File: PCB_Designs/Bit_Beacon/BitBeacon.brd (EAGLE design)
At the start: 30.5 x 33 mm, 105 parts, among them IC1 AD8603UJ, IC2 AD8603UJ, IC3 AD8603UJ, IC4 AD8603UJ

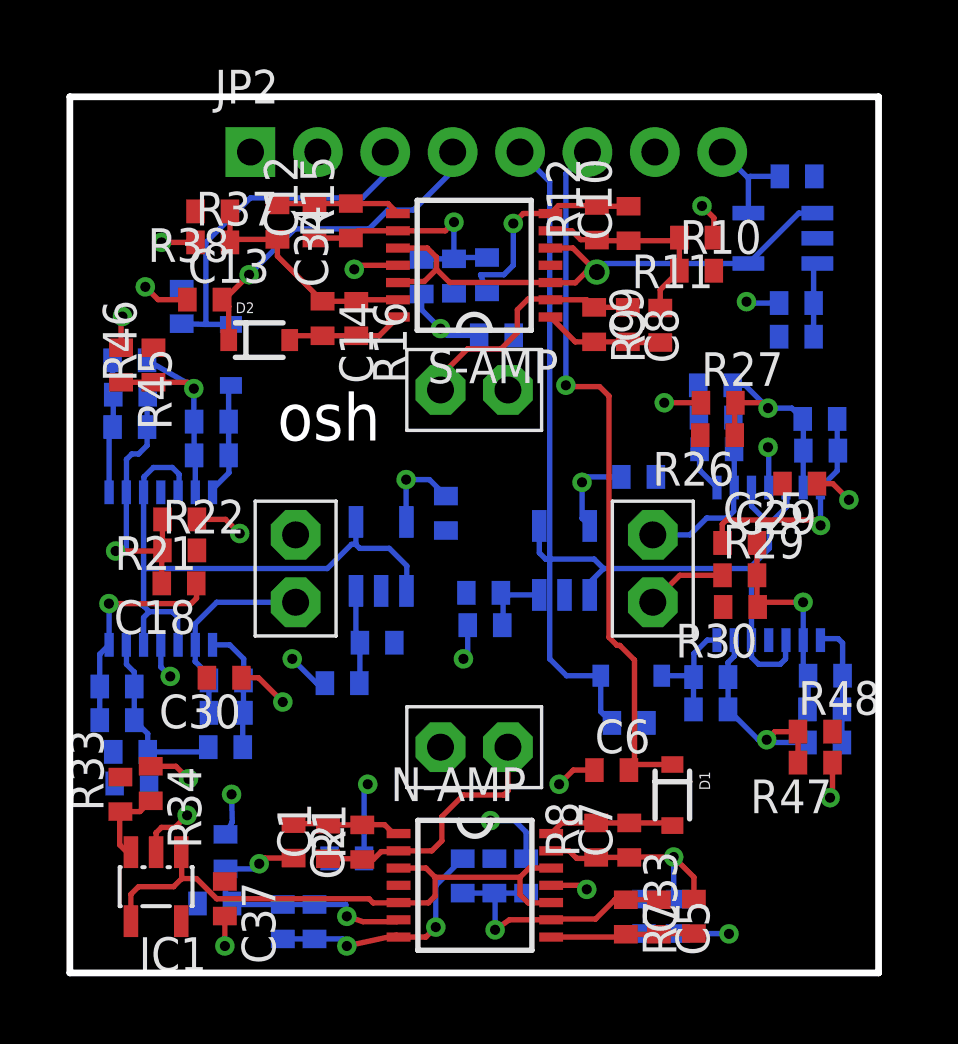
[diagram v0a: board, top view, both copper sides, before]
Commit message: finished and ordered PCB design for Bit Beacon
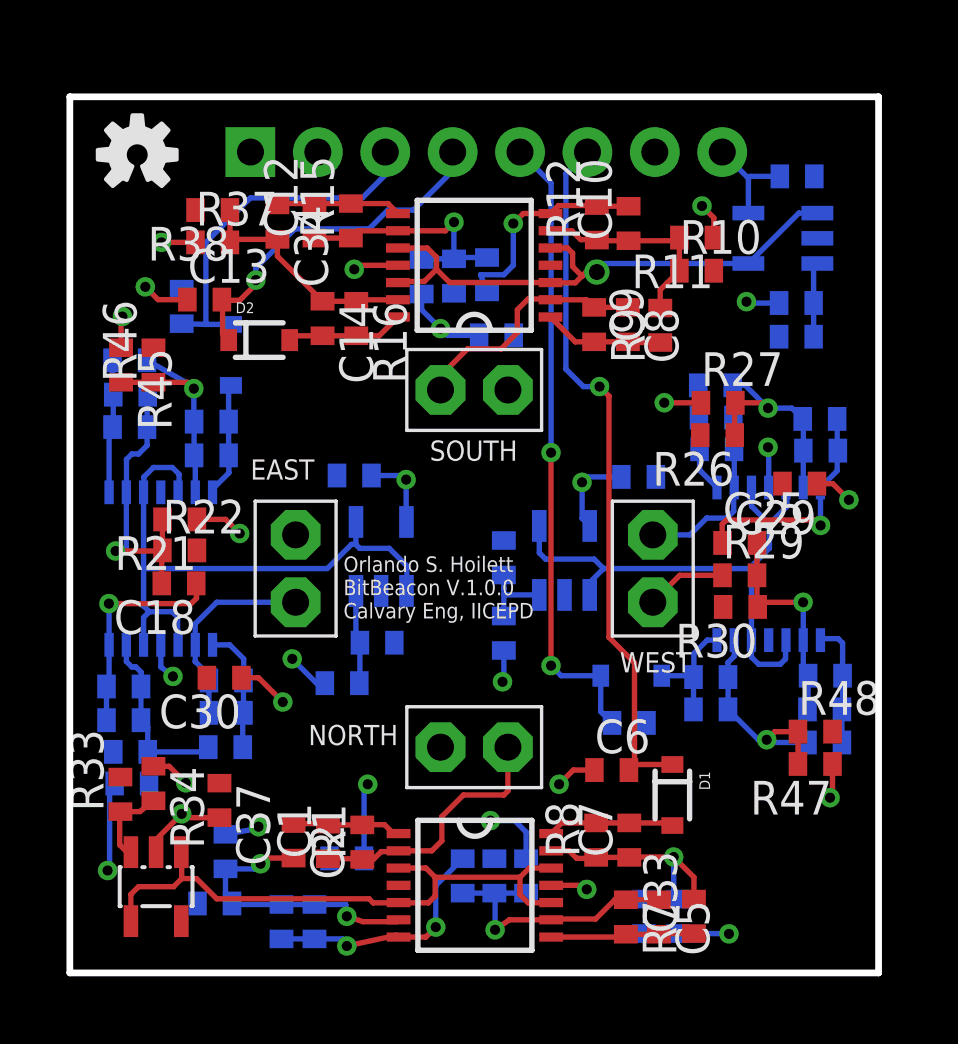
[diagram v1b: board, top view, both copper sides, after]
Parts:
- added LOGO1: OSHW-LOGOS, SparkFun-Aesthetics:OSHW-LOGO-S
- moved C39 3.74 mm to (10.7, 18.7), turned to 0 degrees
- moved C37 3.71 mm to (5.64, 6.50)
- moved R44 1.52 mm to (16.4, 15.6), turned to 270 degrees
- moved R43 0.77 mm to (16.4, 12.8), turned to 270 degrees
- moved C17 0.25 mm to (2.03, 10.8)
- moved R20 0.25 mm to (2.03, 9.53)
- moved R34 0.10 mm to (3.15, 7.14)
- moved C3 0.05 mm to (7.98, 1.93)
- moved R47 0.05 mm to (28.1, 7.87)
- moved R38 0.05 mm to (5.38, 28.8)
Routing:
- net 5V: track 29.8 -> 32.6 mm, vias 12 -> 13
- net GND: track 26.2 -> 26.1 mm, vias 15 -> 14
- net W-OUT: track 23.7 -> 23.8 mm, vias 0 -> 2
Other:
- board text added: "EAST"
- board text added: "NORTH"
- board text added: "Orlando S. Hoilett BitBeacon V.1.0.0 Calvary Eng, IICEPD"
- board text added: "SOUTH"
- board text added: "WEST"
- board text removed: "osh"

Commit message: updating BitBeacon design with a better high pass filter design and started teh BitBeacon_Emitter circuit
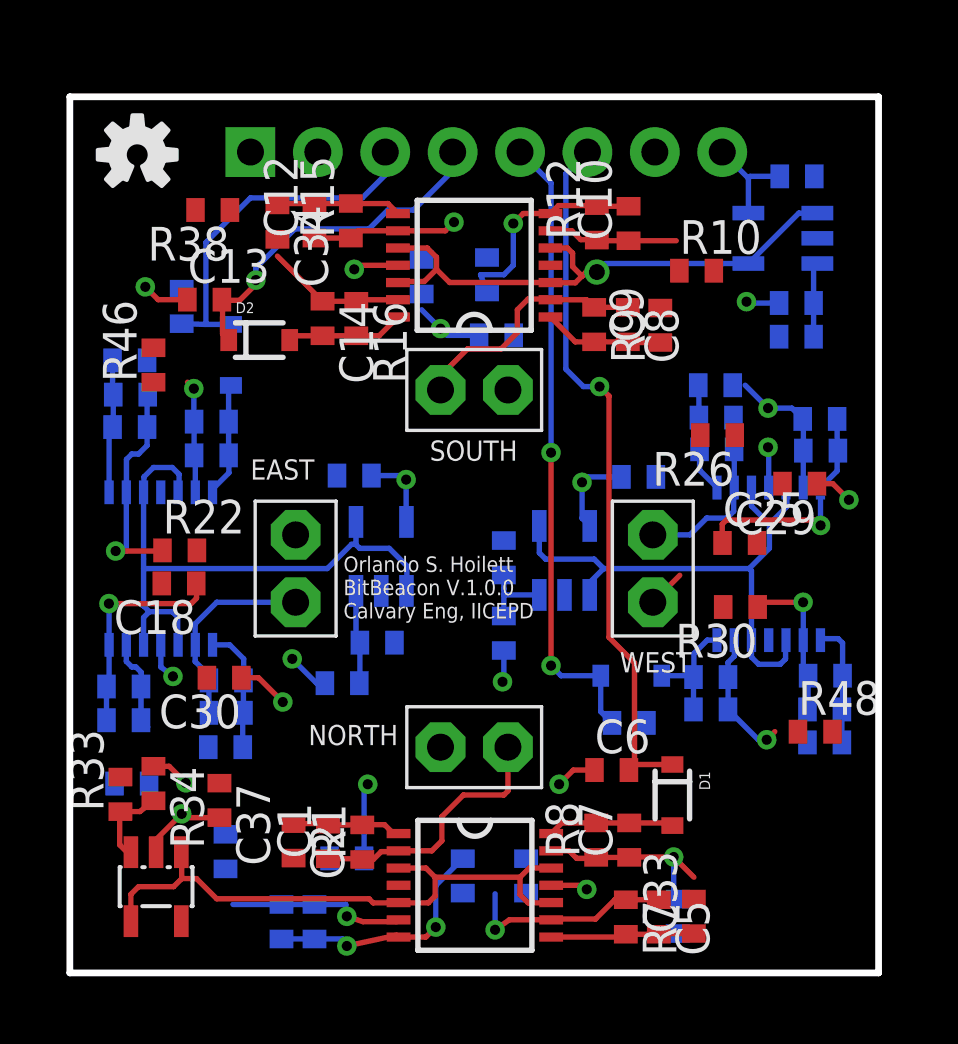
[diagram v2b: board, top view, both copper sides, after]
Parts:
- removed R11, R13, R19, R21, R27, R29, R3, R35, R37, R45, R47, R5: (no value), resistor:R0402
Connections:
- new net N$27: C2.2, R2.2
- new net N$34: C4.2, R6.2
- new net N$35: C33.2, R36.2
- new net N$36: C34.2, R38.2
- new net N$37: C11.2, R14.2
- new net N$38: C9.2, R10.2
- new net N$39: C35.2, R46.2
- new net N$40: C18.2, R22.2
- new net N$41: C16.2, R18.2
- new net N$42: C36.2, R48.2
- new net N$43: C25.2, R30.2
- new net N$45: C23.2, R26.2
- net 5V: no longer R10.2, R14.2, R18.2, R2.2, R22.2, R26.2, R30.2, R36.2, R38.2, R46.2, R48.2, R6.2
- net GND: no longer R11.1, R13.1, R19.1, R21.1, R27.1, R29.1, R3.1, R35.1, R37.1, R45.1, R47.1, R5.1
- net N$10: no longer C33.2, R35.2
- net N$12: no longer C9.2, R11.2
- net N$14: no longer C11.2, R13.2
- net N$2: no longer C34.2, R37.2
- net N$21: no longer C16.2, R19.2
- net N$23: no longer C18.2, R21.2
- net N$25: no longer C36.2, R47.2
- net N$26: no longer C35.2, R45.2
- net N$30: no longer C23.2, R27.2
- net N$32: no longer C25.2, R29.2
- net N$5: no longer C2.2, R3.2
- net N$7: no longer C4.2, R5.2
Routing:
- net GND: track 26.1 -> 16.1 mm, vias 14 -> 8
- net 5V: track 32.6 -> 22.7 mm, vias 13 -> 9
- net N$21: track 8.02 -> 3.53 mm
- net N$26: track 8.84 -> 4.48 mm
- net N$5: track 10.9 -> 6.71 mm, vias 2 -> 1
- net N$14: track 9.38 -> 5.51 mm
- net N$2: track 8.95 -> 5.27 mm
- net N$25: track 8.82 -> 5.29 mm
- net N$12: track 8.01 -> 4.90 mm
- net N$30: track 8.31 -> 5.58 mm
- net N$32: track 8.34 -> 5.66 mm
- net N$7: track 10.4 -> 7.96 mm
- net N$23: track 10.9 -> 8.51 mm
- net N$10: track 9.58 -> 7.27 mm
